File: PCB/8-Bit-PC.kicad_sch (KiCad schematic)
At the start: 28 parts, among them J1 USB_C_Receptacle_PowerOnly_6P

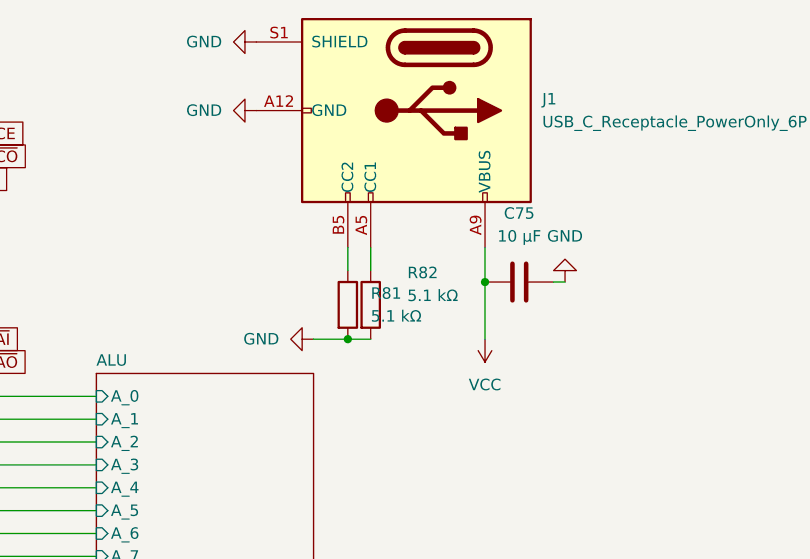
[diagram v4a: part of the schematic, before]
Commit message: Redoing PCB layout and fixed some signal flow convention errors
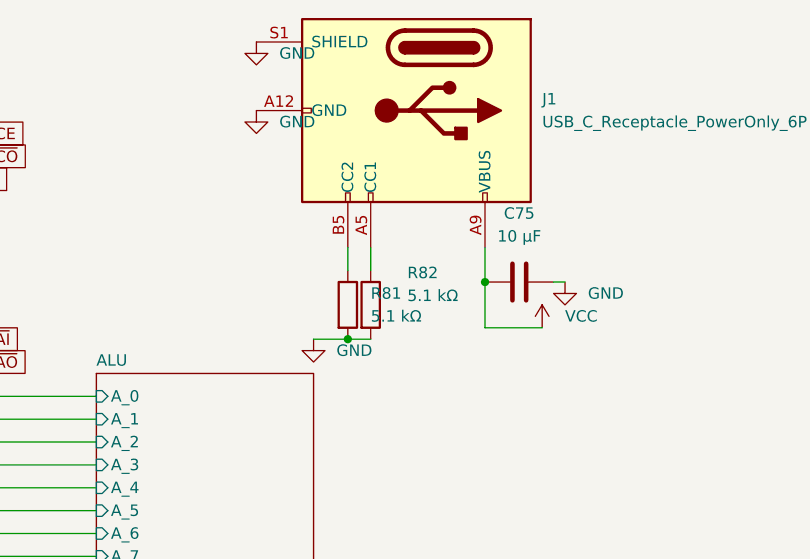
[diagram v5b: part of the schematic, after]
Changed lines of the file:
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@@
 	(wire
 		(pts
-			(xy 184.15 45.72) (xy 184.15 52.07)
-		)
-		(stroke
-			(width 0)
-			(type default)
-		)
-	)
-	(wire
-		(pts
 			(xy 21.59 76.2) (xy 30.48 76.2)
 		)
@@
 	(wire
 		(pts
+			(xy 184.15 50.8) (xy 184.15 45.72)
+		)
+		(stroke
+			(width 0)
+			(type default)
+		)
+	)
+	(wire
+		(pts
 			(xy 24.13 73.66) (xy 30.48 73.66)
 		)
@@
 	(wire
 		(pts
+			(xy 190.5 50.8) (xy 184.15 50.8)
+		)
+		(stroke
+			(width 0)
+			(type default)
+		)
+	)
+	(wire
+		(pts
 			(xy 58.42 180.34) (xy 62.23 180.34)
 		)
@@
 	(symbol
 		(lib_id "power:GND")
-		(at 193.04 45.72 180)
+		(at 193.04 45.72 0)
 		(unit 1)
 		(exclude_from_sim no)
@@
 		(fields_autoplaced yes)
 		(property "Reference" "#PWR0220"
-			(at 193.04 39.37 0)
+			(at 193.04 52.07 0)
 			(effects
 				(font
@@
 		)
 		(property "Value" "GND"
-			(at 193.04 40.64 0)
+			(at 195.58 46.9899 0)
 			(effects
 				(font
 					(size 1.27 1.27)
 				)
+				(justify left)
 			)
 		)
@@
 	(symbol
 		(lib_id "power:GND")
-		(at 165.1 52.07 270)
+		(at 165.1 52.07 0)
 		(unit 1)
 		(exclude_from_sim no)
@@
 		(fields_autoplaced yes)
 		(property "Reference" "#PWR0102"
-			(at 158.75 52.07 0)
+			(at 165.1 58.42 0)
 			(effects
 				(font
@@
 		)
 		(property "Value" "GND"
-			(at 161.29 52.0699 90)
+			(at 167.64 53.3399 0)
 			(effects
 				(font
 					(size 1.27 1.27)
 				)
-				(justify right)
+				(justify left)
 			)
 		)
@@
 	(symbol
 		(lib_id "power:VCC")
-		(at 184.15 52.07 180)
+		(at 190.5 50.8 0)
 		(unit 1)
 		(exclude_from_sim no)
@@
 		(fields_autoplaced yes)
 		(property "Reference" "#PWR0104"
-			(at 184.15 48.26 0)
+			(at 190.5 54.61 0)
 			(effects
 				(font
@@
 		)
 		(property "Value" "VCC"
-			(at 184.15 57.15 0)
+			(at 193.04 49.5299 0)
 			(effects
 				(font
 					(size 1.27 1.27)
 				)
+				(justify left)
 			)
 		)
 		(property "Footprint" ""
-			(at 184.15 52.07 0)
+			(at 190.5 50.8 0)
 			(effects
 				(font
@@
 		)
 		(property "Datasheet" ""
-			(at 184.15 52.07 0)
+			(at 190.5 50.8 0)
 			(effects
 				(font
@@
 		)
 		(property "Description" "Power symbol creates a global label with name \"VCC\""
-			(at 184.15 52.07 0)
+			(at 190.5 50.8 0)
 			(effects
 				(font
@@
 	(symbol
 		(lib_id "power:GND")
-		(at 158.75 26.67 270)
+		(at 158.75 26.67 0)
 		(unit 1)
 		(exclude_from_sim no)
@@
 		(fields_autoplaced yes)
 		(property "Reference" "#PWR0103"
-			(at 152.4 26.67 0)
+			(at 158.75 33.02 0)
 			(effects
 				(font
@@
 		)
 		(property "Value" "GND"
-			(at 154.94 26.6699 90)
+			(at 161.29 27.9399 0)
 			(effects
 				(font
 					(size 1.27 1.27)
 				)
-				(justify right)
+				(justify left)
 			)
 		)
@@
 	(symbol
 		(lib_id "power:GND")
-		(at 158.75 19.05 270)
+		(at 158.75 19.05 0)
 		(unit 1)
 		(exclude_from_sim no)
@@
 		(fields_autoplaced yes)
 		(property "Reference" "#PWR0105"
-			(at 152.4 19.05 0)
+			(at 158.75 25.4 0)
 			(effects
 				(font
@@
 		)
 		(property "Value" "GND"
-			(at 154.94 19.0499 90)
+			(at 161.29 20.3199 0)
 			(effects
 				(font
 					(size 1.27 1.27)
 				)
-				(justify right)
+				(justify left)
 			)
 		)

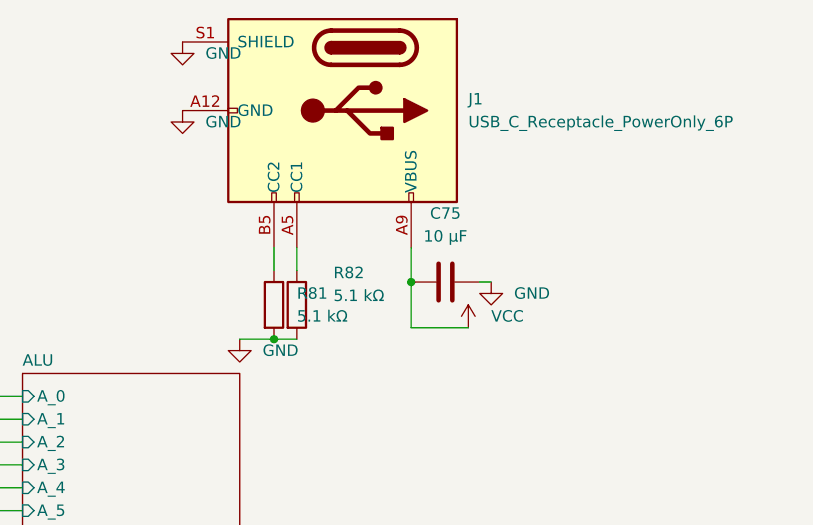
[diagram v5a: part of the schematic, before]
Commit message: backing up before routing for easily going back if i mess up
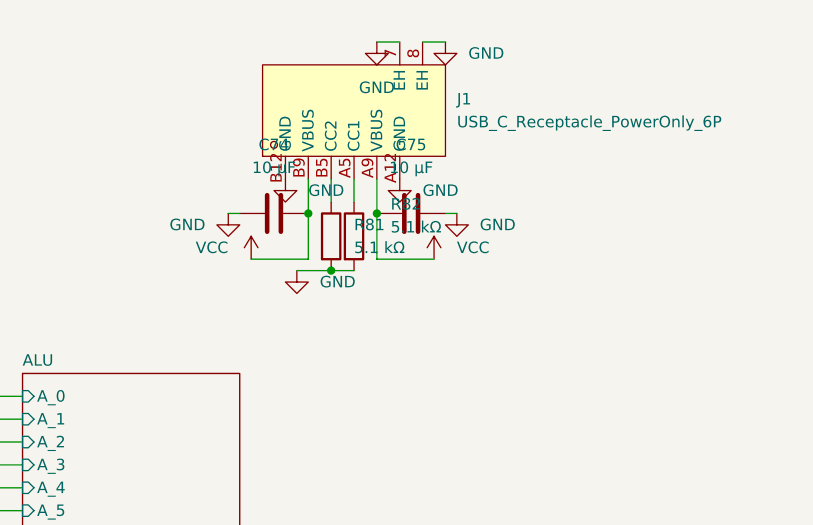
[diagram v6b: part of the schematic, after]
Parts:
- added C74: 10 µF, Capacitor_THT:C_Radial_D5.0mm_H5.0mm_P2.00mm, symbol Device:C
- J1: footprint Connector_USB:USB_C_Receptacle_HRO_TYPE-C-31-M-17 -> easyeda2kicad:USB-TH_TYPE-C-6P-LCH10.0; symbol Connector:USB_C_Receptacle_PowerOnly_6P -> easyeda2kicad:TYPE-C6PLCH10.0; LCSC Part (none) -> C5187470
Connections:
- net GND: now also J1.7 (EH), J1.8 (EH), C74.2; no longer J1.S1 (SHIELD)
- net VCC: now also C74.1
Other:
- moved on the sheet: C75, R81, R82
